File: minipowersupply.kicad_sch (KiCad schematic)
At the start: 0 parts

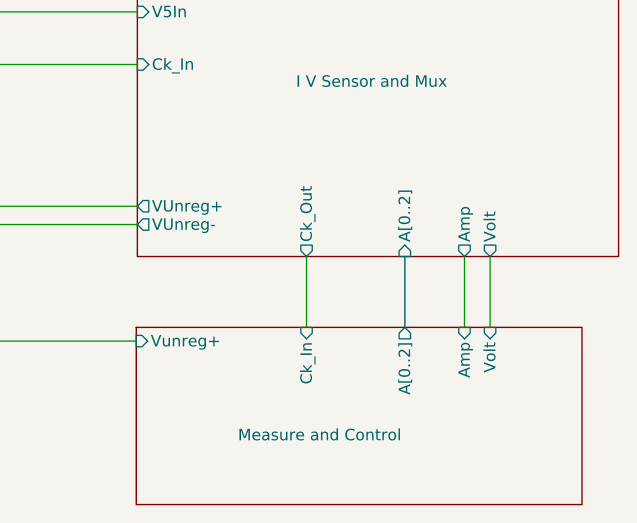
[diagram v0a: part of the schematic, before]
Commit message: further refining board size, adding rotary encoder and OLED display
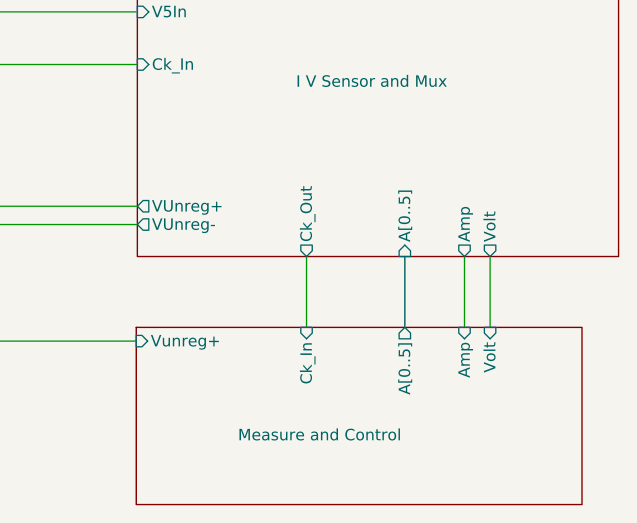
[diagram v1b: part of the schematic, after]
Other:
- sheet I V Sensor and Mux ports: added A[0..5]; removed A[0..2]
- sheet Measure and Control ports: added A[0..5]; removed A[0..2]
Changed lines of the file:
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@@
       (effects (font (size 1.27 1.27)) (justify left))
     )
-    (pin "A[0..2]" output (at 213.233 122.682 90)
+    (pin "A[0..5]" output (at 213.233 122.682 90)
       (effects (font (size 1.27 1.27)) (justify right))
     )
@@
       (effects (font (size 1.27 1.27)) (justify left top) hide)
     )
-    (pin "A[0..2]" input (at 213.233 114.808 270)
+    (pin "A[0..5]" input (at 213.233 114.808 270)
       (effects (font (size 1.27 1.27)) (justify left))
     )
@@
       (reference "#PWR013") (unit 1) (value "GNDREF") (footprint "")
     )
+    (path "/e84becbb-d7bb-4f82-b4d3-8ddac9da005f/68bac005-c738-4ad4-aaaf-99ec32852977"
+      (reference "#PWR014") (unit 1) (value "GNDREF") (footprint "")
+    )
+    (path "/e84becbb-d7bb-4f82-b4d3-8ddac9da005f/d30398c4-56ff-456f-8bcd-6abe3278f157"
+      (reference "#PWR015") (unit 1) (value "GNDREF") (footprint "")
+    )
+    (path "/e84becbb-d7bb-4f82-b4d3-8ddac9da005f/6de4e81c-7297-48a2-9c4d-71a45ddded8b"
+      (reference "#PWR016") (unit 1) (value "GNDREF") (footprint "")
+    )
     (path "/f603f830-1954-4cf1-9214-ed1b9cc75116/245637c0-5a2f-45d2-bb02-961552ae7129"
       (reference "#PWR017") (unit 1) (value "GNDREF") (footprint "")
@@
       (reference "#PWR023") (unit 1) (value "GNDREF") (footprint "")
     )
+    (path "/e84becbb-d7bb-4f82-b4d3-8ddac9da005f/b750a0a8-968b-4922-95d0-6009d99584f8"
+      (reference "#PWR024") (unit 1) (value "GNDREF") (footprint "")
+    )
     (path "/04da8333-1ee2-480f-9c82-cd475e7d9e9d/76494575-5efa-4cbe-baf9-9ba6187bfe0a"
       (reference "#PWR025") (unit 1) (value "GNDREF") (footprint "")
@@
       (reference "#PWR031") (unit 1) (value "GNDREF") (footprint "")
     )
-    (path "/e84becbb-d7bb-4f82-b4d3-8ddac9da005f/e9ba396a-a163-47a4-ab75-2eecdc16696a"
-      (reference "#PWR032") (unit 1) (value "GNDREF") (footprint "")
-    )
     (path "/f603f830-1954-4cf1-9214-ed1b9cc75116/9e49a0e5-227d-4a50-a1e1-04e81c4e4cef/4496cfa9-1f5e-49b8-b439-1895b1d3b362"
       (reference "#PWR033") (unit 1) (value "GNDREF") (footprint "")
@@
       (reference "#PWR0102") (unit 1) (value "GNDREF") (footprint "")
     )
+    (path "/e84becbb-d7bb-4f82-b4d3-8ddac9da005f/bba79f71-054d-48e3-a6f8-578855d54f6b"
+      (reference "#PWR0103") (unit 1) (value "GNDREF") (footprint "")
+    )
     (path "/e84becbb-d7bb-4f82-b4d3-8ddac9da005f/e18d8df6-911d-4892-87af-96bc187d73d0"
       (reference "A1") (unit 1) (value "Arduino_Nano_v3.x") (footprint "Module:Arduino_Nano")
@@
       (reference "C13") (unit 1) (value "0.1uF") (footprint "Capacitor_SMD:C_0603_1608Metric")
     )
+    (path "/e84becbb-d7bb-4f82-b4d3-8ddac9da005f/5b834e9d-9412-4b32-a2e2-49131148b65a"
+      (reference "C14") (unit 1) (value "0.1uF") (footprint "Capacitor_SMD:C_0603_1608Metric")
+    )
+    (path "/e84becbb-d7bb-4f82-b4d3-8ddac9da005f/dbceb944-7f89-45f0-bf3c-265591aa50ed"
+      (reference "C15") (unit 1) (value "0.1uF") (footprint "Capacitor_SMD:C_0603_1608Metric")
+    )
+    (path "/e84becbb-d7bb-4f82-b4d3-8ddac9da005f/e37b5d37-16fb-493d-8379-6c8eb40ea48b"
+      (reference "C16") (unit 1) (value "0.1uF") (footprint "Capacitor_SMD:C_0603_1608Metric")
+    )
     (path "/f603f830-1954-4cf1-9214-ed1b9cc75116/e02e7160-6e58-4844-8bf5-047dcc9f99ea"
       (reference "C17") (unit 1) (value "0.1uF") (footprint "Capacitor_SMD:C_0603_1608Metric")
@@
       (reference "C33") (unit 1) (value "0.1uF") (footprint "Capacitor_SMD:C_0603_1608Metric")
     )
+    (path "/e84becbb-d7bb-4f82-b4d3-8ddac9da005f/4323e4f2-03fa-4621-8b6b-1af0874ec8df"
+      (reference "C34") (unit 1) (value "0.1uF") (footprint "Capacitor_SMD:C_0603_1608Metric")
+    )
     (path "/f603f830-1954-4cf1-9214-ed1b9cc75116/b0d622a9-3316-43e0-a924-cdea4dccff2a/870f3584-8a2b-410b-bc98-e5cb95c118a7"
       (reference "C35") (unit 1) (value "0.1uF") (footprint "Capacitor_SMD:C_0603_1608Metric")
@@
       (reference "D9") (unit 1) (value "S1K-13-F") (footprint "Diode_SMD:D_SMA")
     )
-    (path "/e84becbb-d7bb-4f82-b4d3-8ddac9da005f/75909ddd-26b9-4e79-807a-365005e91861"
-      (reference "DS1") (unit 1) (value "OLED-128O064D") (footprint "Display:OLED-128O064D")
-    )
     (path "/0171d92e-8d18-4439-a831-c9696203c470/b70ffcfb-e42e-4e3a-8bd2-47d191d0fca1"
       (reference "F1") (unit 1) (value "Fuse") (footprint "Fuse:Fuseholder_Cylinder-5x20mm_Bulgin_FX0457_Horizontal_Closed")
@@
       (reference "J9") (unit 1) (value "Conn_01x02_Female") (footprint "Connector_PinHeader_2.54mm:PinHeader_1x02_P2.54mm_Vertical")
     )
+    (path "/e84becbb-d7bb-4f82-b4d3-8ddac9da005f/772055d4-fd88-4274-bb55-5b313f2a1265"
+      (reference "J10") (unit 1) (value "Conn_01x30_Male") (footprint "WE SMD Side 30 Pin:687130149022")
+    )
     (path "/04da8333-1ee2-480f-9c82-cd475e7d9e9d/66b966a8-357f-4588-9d64-e40b9b2d82bc"
       (reference "Q1") (unit 1) (value "BC817") (footprint "Package_TO_SOT_SMD:SOT-23")
@@
       (reference "R20") (unit 1) (value "10k") (footprint "Resistor_SMD:R_0603_1608Metric")
     )
+    (path "/e84becbb-d7bb-4f82-b4d3-8ddac9da005f/a6e03dd3-87e1-4375-af43-bb3d3f653955"
+      (reference "R21") (unit 1) (value "10k") (footprint "Resistor_SMD:R_0603_1608Metric")
+    )
+    (path "/e84becbb-d7bb-4f82-b4d3-8ddac9da005f/3ff46b3a-1ebb-47b5-96b8-6c72be309816"
+      (reference "R22") (unit 1) (value "10k") (footprint "Resistor_SMD:R_0603_1608Metric")
+    )
+    (path "/e84becbb-d7bb-4f82-b4d3-8ddac9da005f/02d68b5e-d191-47cb-b7c0-e0348d6e8e6a"
+      (reference "R23") (unit 1) (value "10k") (footprint "Resistor_SMD:R_0603_1608Metric")
+    )
+    (path "/e84becbb-d7bb-4f82-b4d3-8ddac9da005f/6a841186-6643-4888-8f07-48585c95e9fc"
+      (reference "R24") (unit 1) (value "10k") (footprint "Resistor_SMD:R_0603_1608Metric")
+    )
+    (path "/e84becbb-d7bb-4f82-b4d3-8ddac9da005f/dcf798aa-d663-43c4-9ba1-8bde70a5592e"
+      (reference "R25") (unit 1) (value "10k") (footprint "Resistor_SMD:R_0603_1608Metric")
+    )
+    (path "/e84becbb-d7bb-4f82-b4d3-8ddac9da005f/e6667ba4-7e55-47df-9ea6-3ab763c8ff2f"
+      (reference "R26") (unit 1) (value "10k") (footprint "Resistor_SMD:R_0603_1608Metric")
+    )
     (path "/ad7d34fc-ea53-4304-ba5f-b50b36043af6/ffb63565-cbf3-4724-bc54-d6a7b5aa1900"
       (reference "RV1") (unit 1) (value "5k") (footprint "")
@@
       (reference "RV2") (unit 1) (value "5k") (footprint "")
     )
+    (path "/e84becbb-d7bb-4f82-b4d3-8ddac9da005f/23311901-7468-4bf4-aafc-bbb1c10a97fd"
+      (reference "SW1") (unit 1) (value "RotaryEncoder_Switch") (footprint "Rotary_Encoder:RotaryEncoder_Alps_EC11E_Vertical_H20mm")
+    )
     (path "/0171d92e-8d18-4439-a831-c9696203c470/6f0fe44a-f55d-46f7-974a-ed9861cce930"

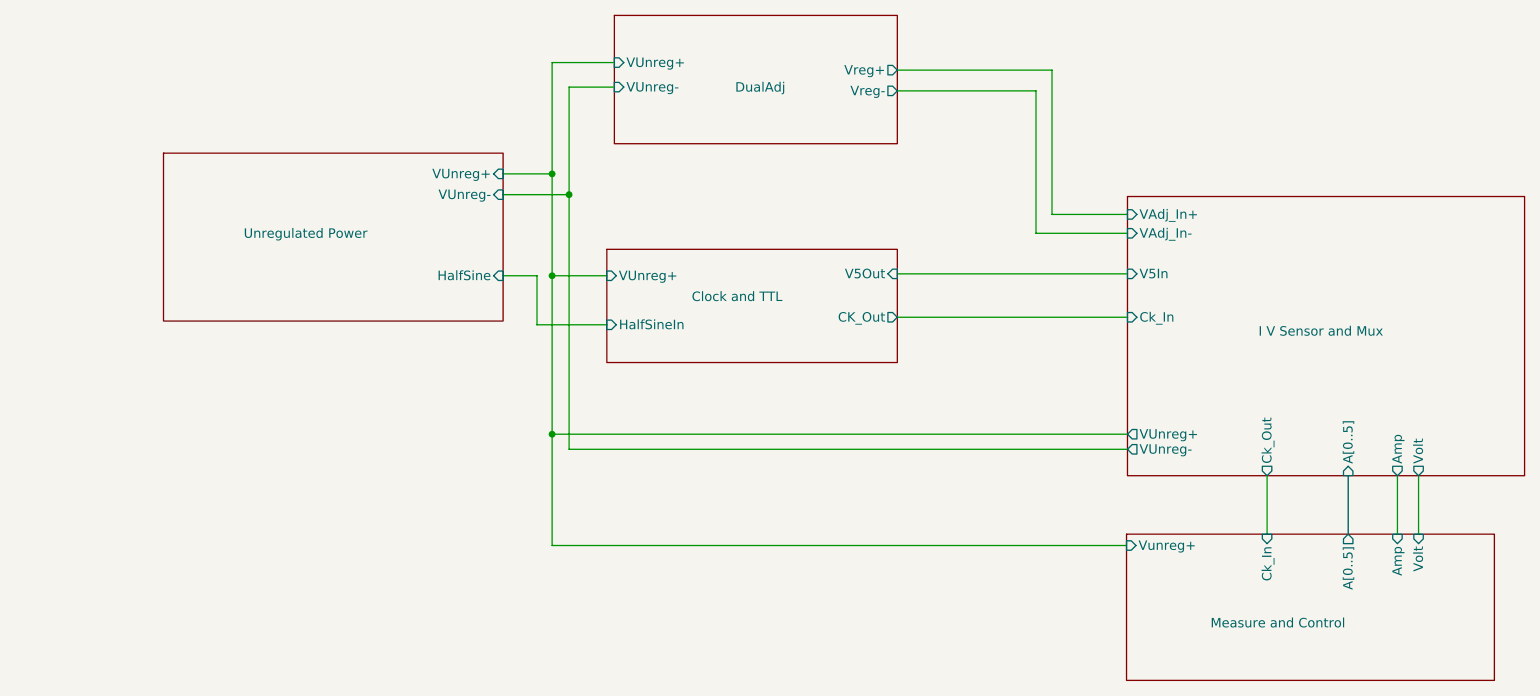
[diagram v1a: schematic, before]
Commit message: repositioned signal wires and started mapping OLED and rotary encoder
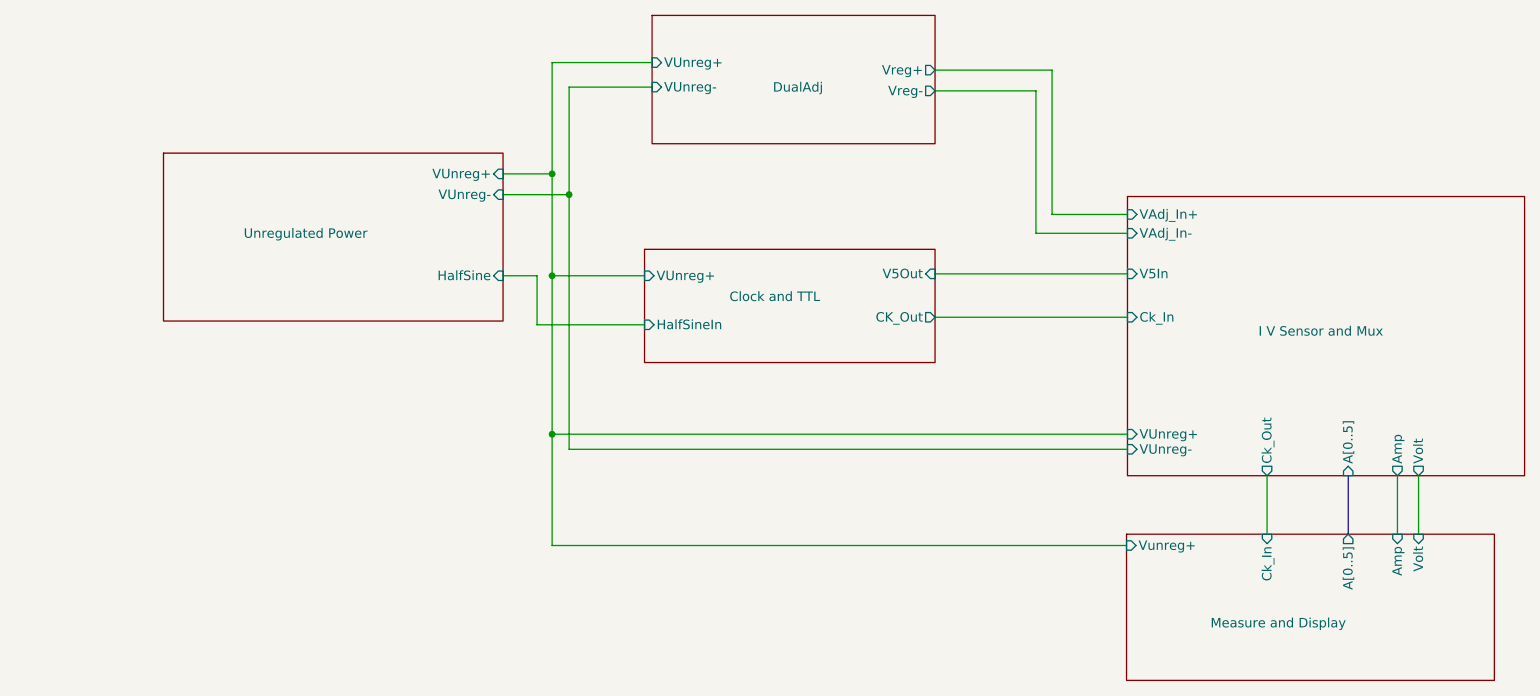
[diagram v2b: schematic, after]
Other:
- sheet Measure and Control renamed Measure and Display
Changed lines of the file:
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@@
   (junction (at 106.045 74.168) (diameter 0) (color 0 0 0 0)
   )
-  (wire (pts (xy 152.527 87.63) (xy 183.515 87.63))
+  (wire (pts (xy 157.607 87.63) (xy 183.515 87.63))
     (stroke (width 0) (type default) (color 0 0 0 0))
   )
@@
     (stroke (width 0) (type default) (color 0 0 0 0))
   )
-  (wire (pts (xy 171.196 62.992) (xy 152.527 62.992))
-    (stroke (width 0) (type default) (color 0 0 0 0))
-  )
-  (wire (pts (xy 152.527 93.472) (xy 183.515 93.472))
-    (stroke (width 0) (type default) (color 0 0 0 0))
-  )
-  (wire (pts (xy 106.045 87.884) (xy 113.411 87.884))
+  (wire (pts (xy 171.196 62.992) (xy 157.607 62.992))
+    (stroke (width 0) (type default) (color 0 0 0 0))
+  )
+  (wire (pts (xy 157.607 93.472) (xy 183.515 93.472))
+    (stroke (width 0) (type default) (color 0 0 0 0))
+  )
+  (wire (pts (xy 106.045 87.884) (xy 118.491 87.884))
     (stroke (width 0) (type default) (color 0 0 0 0))
   )
@@
     (stroke (width 0) (type default) (color 0 0 0 0))
   )
-  (wire (pts (xy 152.527 60.198) (xy 173.355 60.198))
+  (wire (pts (xy 157.607 60.198) (xy 173.355 60.198))
     (stroke (width 0) (type default) (color 0 0 0 0))
   )
@@
     (stroke (width 0) (type default) (color 0 0 0 0))
   )
-  (wire (pts (xy 113.411 94.488) (xy 104.013 94.488))
+  (wire (pts (xy 118.491 94.488) (xy 104.013 94.488))
     (stroke (width 0) (type default) (color 0 0 0 0))
   )
@@
     (stroke (width 0) (type default) (color 0 0 0 0))
   )
-  (wire (pts (xy 114.427 59.182) (xy 106.045 59.182))
+  (wire (pts (xy 119.507 59.182) (xy 106.045 59.182))
     (stroke (width 0) (type default) (color 0 0 0 0))
   )
@@
     (stroke (width 0) (type default) (color 0 0 0 0))
   )
-  (wire (pts (xy 114.427 62.484) (xy 108.331 62.484))
+  (wire (pts (xy 119.507 62.484) (xy 108.331 62.484))
     (stroke (width 0) (type default) (color 0 0 0 0))
   )
@@
     )
   )
-  (sheet (at 113.411 84.328) (size 39.116 15.24)
-    (stroke (width 0.1524) (type solid) (color 0 0 0 0))
-    (fill (color 0 0 0 0.0000))
-    (property "Sheet name" "Clock and TTL" (id 0) (at 124.841 91.44 0)
-      (effects (font (size 1.27 1.27)) (justify left bottom))
-    )
-    (property "Sheet file" "CKTTL.kicad_sch" (id 1) (at 113.411 100.1526 0)
-      (effects (font (size 1.27 1.27)) (justify left top) hide)
-    )
-    (pin "HalfSineIn" input (at 113.411 94.488 180)
-      (effects (font (size 1.27 1.27)) (justify left))
-    )
-    (pin "V5Out" input (at 152.527 87.63 0)
-      (effects (font (size 1.27 1.27)) (justify right))
-    )
-    (pin "VUnreg+" input (at 113.411 87.884 180)
-      (effects (font (size 1.27 1.27)) (justify left))
-    )
-    (pin "CK_Out" output (at 152.527 93.472 0)
-      (effects (font (size 1.27 1.27)) (justify right))
-    )
-  )
-  (sheet (at 114.427 52.832) (size 38.1 17.272)
-    (stroke (width 0.1524) (type solid) (color 0 0 0 0))
-    (fill (color 0 0 0 0.0000))
-    (property "Sheet name" "DualAdj" (id 0) (at 130.683 63.246 0)
-      (effects (font (size 1.27 1.27)) (justify left bottom))
-    )
-    (property "Sheet file" "dualadj.kicad_sch" (id 1) (at 114.427 70.6886 0)
-      (effects (font (size 1.27 1.27)) (justify left top) hide)
-    )
-    (pin "VUnreg-" input (at 114.427 62.484 180)
-      (effects (font (size 1.27 1.27)) (justify left))
-    )
-    (pin "VUnreg+" input (at 114.427 59.182 180)
-      (effects (font (size 1.27 1.27)) (justify left))
-    )
-    (pin "Vreg+" output (at 152.527 60.198 0)
-      (effects (font (size 1.27 1.27)) (justify right))
-    )
-    (pin "Vreg-" output (at 152.527 62.992 0)
+  (sheet (at 118.491 84.328) (size 39.116 15.24)
+    (stroke (width 0.1524) (type solid) (color 0 0 0 0))
+    (fill (color 0 0 0 0.0000))
+    (property "Sheet name" "Clock and TTL" (id 0) (at 129.921 91.44 0)
+      (effects (font (size 1.27 1.27)) (justify left bottom))
+    )
+    (property "Sheet file" "CKTTL.kicad_sch" (id 1) (at 118.491 100.1526 0)
+      (effects (font (size 1.27 1.27)) (justify left top) hide)
+    )
+    (pin "HalfSineIn" input (at 118.491 94.488 180)
+      (effects (font (size 1.27 1.27)) (justify left))
+    )
+    (pin "V5Out" input (at 157.607 87.63 0)
+      (effects (font (size 1.27 1.27)) (justify right))
+    )
+    (pin "VUnreg+" input (at 118.491 87.884 180)
+      (effects (font (size 1.27 1.27)) (justify left))
+    )
+    (pin "CK_Out" output (at 157.607 93.472 0)
+      (effects (font (size 1.27 1.27)) (justify right))
+    )
+  )
+  (sheet (at 119.507 52.832) (size 38.1 17.272)
+    (stroke (width 0.1524) (type solid) (color 0 0 0 0))
+    (fill (color 0 0 0 0.0000))
+    (property "Sheet name" "DualAdj" (id 0) (at 135.763 63.246 0)
+      (effects (font (size 1.27 1.27)) (justify left bottom))
+    )
+    (property "Sheet file" "dualadj.kicad_sch" (id 1) (at 119.507 70.6886 0)
+      (effects (font (size 1.27 1.27)) (justify left top) hide)
+    )
+    (pin "VUnreg-" input (at 119.507 62.484 180)
+      (effects (font (size 1.27 1.27)) (justify left))
+    )
+    (pin "VUnreg+" input (at 119.507 59.182 180)
+      (effects (font (size 1.27 1.27)) (justify left))
+    )
+    (pin "Vreg+" output (at 157.607 60.198 0)
+      (effects (font (size 1.27 1.27)) (justify right))
+    )
+    (pin "Vreg-" output (at 157.607 62.992 0)
       (effects (font (size 1.27 1.27)) (justify right))
     )
@@
     (stroke (width 0.1524) (type solid) (color 0 0 0 0))
     (fill (color 0 0 0 0.0000))
-    (property "Sheet name" "Measure and Control" (id 0) (at 194.691 135.382 0)
+    (property "Sheet name" "Measure and Display" (id 0) (at 194.691 135.382 0)
       (effects (font (size 1.27 1.27)) (justify left bottom))
     )
@@
       (effects (font (size 1.27 1.27)) (justify left))
     )
-    (pin "VUnreg+" output (at 183.515 109.22 180)
-      (effects (font (size 1.27 1.27)) (justify left))
-    )
-    (pin "VUnreg-" output (at 183.515 111.252 180)
-      (effects (font (size 1.27 1.27)) (justify left))
-    )
+    (pin "VUnreg+" input (at 183.515 109.22 180)
+      (effects (font (size 1.27 1.27)) (justify left))
+    )
+    (pin "VUnreg-" input (at 183.515 111.252 180)
+      (effects (font (size 1.27 1.27)) (justify left))
+    )
